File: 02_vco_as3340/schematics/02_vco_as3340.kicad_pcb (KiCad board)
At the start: 2 copper layers, 75 x 100 mm, 89 parts, among them J1 Header 1, J10 SINE OUT, J2 Header 2, J3 SYNC IN, J4 FM IN, J5 PWM CV IN, J6 1V per O IN, J7 SQUARE OUT, J8 SAW OUT, J9 TRI OUT, Q1 BC547C, Q2 BC547C, U1 TL072, U2 AS3340, U3 TL074

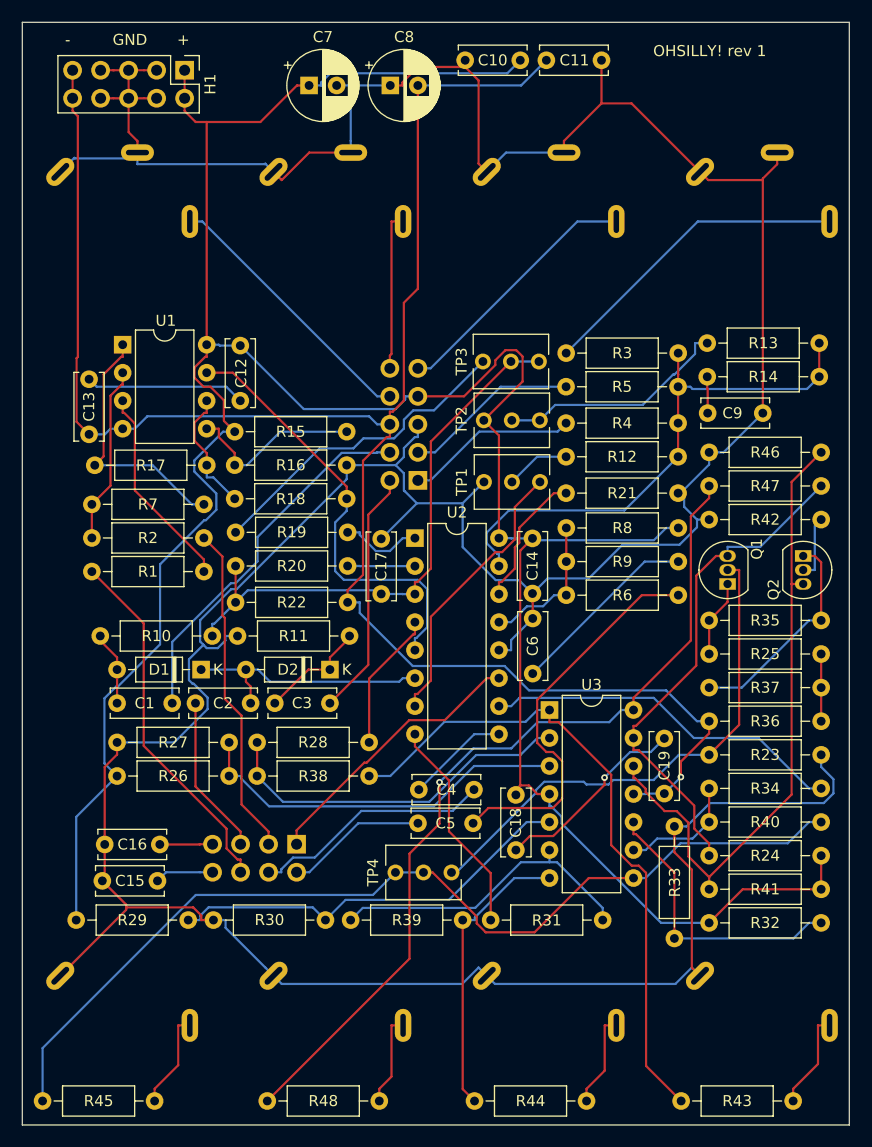
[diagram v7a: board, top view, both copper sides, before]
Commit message: fine-tuned PCB hole distanes
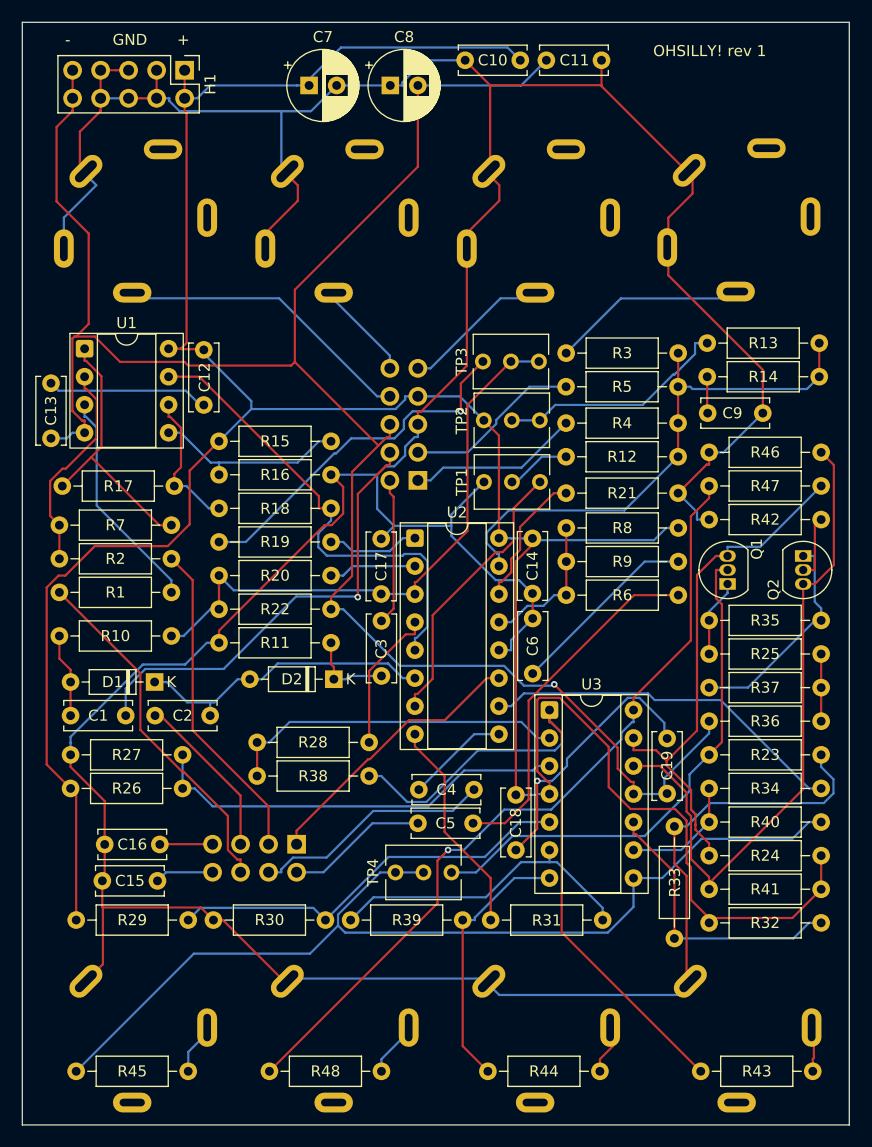
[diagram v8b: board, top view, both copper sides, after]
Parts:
- J10, J7, J8, J9: footprint cynthia:6.35 mm jack socket mono -> cynthia:6.35 mm jack socket mono in 3 pin socket tip pin west
- J3, J4, J5, J6: footprint cynthia:6.35 mm jack socket mono switched -> cynthia:6.35 mm jack socket mono switched in 5 pin socket
- U1: footprint Package_DIP:DIP-8_W7.62mm -> Package_DIP:DIP-8_W7.62mm_Socket
- U2: footprint Package_DIP:DIP-16_W7.62mm -> Package_DIP:DIP-16_W7.62mm_Socket
- U3: footprint Package_DIP:DIP-14_W7.62mm -> Package_DIP:DIP-14_W7.62mm_Socket
- moved C3 9.98 mm to (177.3, 102.8), turned to 90 degrees
- moved D1 4.36 mm to (156.8, 103.3)
- moved C1 4.36 mm to (149.1, 106.4)
- moved R26 4.36 mm to (149.1, 113.0)
- moved R27 4.36 mm to (159.3, 109.9)
- moved R45 4.07 mm to (149.6, 138.6)
- moved C2 3.84 mm to (161.8, 106.4)
- moved R10 3.71 mm to (148.1, 99.1)
- moved R17 3.50 mm to (148.4, 85.5)
- moved R1 3.50 mm to (148.1, 95.2)
- moved R2 3.50 mm to (158.3, 92.1)
- moved R7 3.50 mm to (148.1, 89.1)
- moved C13 3.47 mm to (147.4, 81.2)
- moved U1 3.47 mm to (150.4, 73.1)
- moved C12 3.33 mm to (161.2, 78.2)
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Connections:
- R3 pad 1: Net-(J6-T) -> Net-(J6-PadT)
- R43 pad 2: Net-(J7-T) -> Net-(J7-PadT)
- R44 pad 2: Net-(J8-T) -> Net-(J8-PadT)
- R45 pad 2: Net-(J9-T) -> Net-(J9-PadT)
- R48 pad 2: Net-(J10-T) -> Net-(J10-PadT)
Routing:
- net Net-(J6-T): track 28.8 -> 0.00 mm
- net Net-(J6-PadT): track 0.00 -> 17.5 mm
- net PWM CV Hot: track 23.5 -> 13.3 mm
- net Hard Sync -: track 22.5 -> 13.3 mm
- net Net-(J7-T): track 8.84 -> 0.00 mm
- net Net-(J9-T): track 8.80 -> 0.00 mm
- net Net-(J8-T): track 8.59 -> 0.00 mm
- net Net-(J10-T): track 8.37 -> 0.00 mm
- net +12V: track 252.1 -> 260.0 mm
- net Hard Sync +: track 33.7 -> 41.5 mm, vias 0 -> 1
- net Net-(C18-Pad1): track 18.0 -> 24.5 mm
- net -12V: track 173.3 -> 179.7 mm
- net Net-(R47-Pad2): track 78.8 -> 73.0 mm
- net GND: track 373.5 -> 378.6 mm
- net Net-(J10-PadT): track 0.00 -> 4.83 mm
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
